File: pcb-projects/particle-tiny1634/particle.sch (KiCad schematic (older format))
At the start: 31 parts, among them CON1 AVR-ISP-6, IC1 ATTINY1634-SU, P1 TXN, P2 RXN, P3 TXS, P4 RXS, P5 TRX-CH, P6 TEST1-3

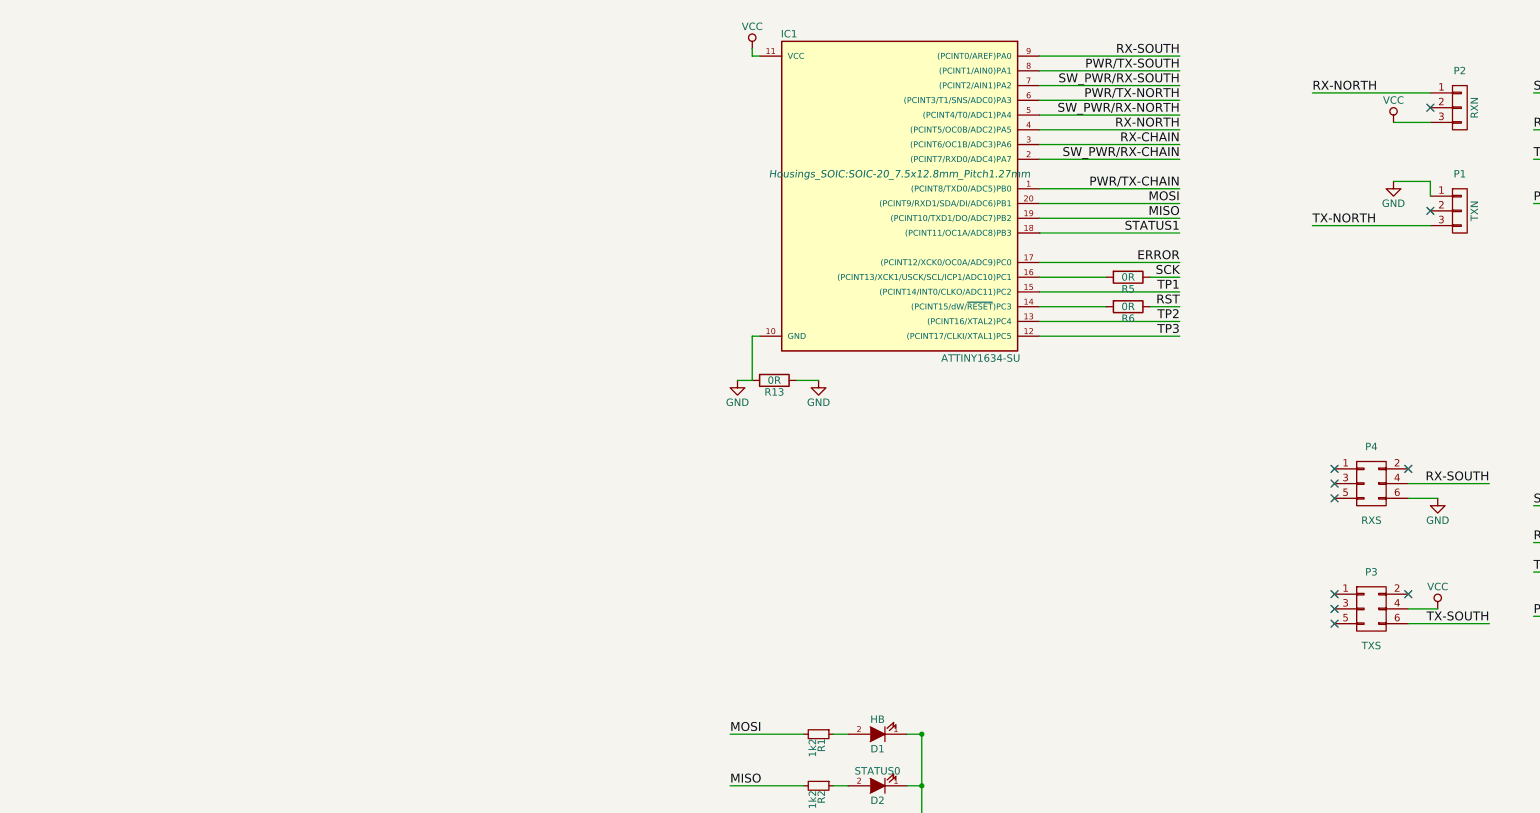
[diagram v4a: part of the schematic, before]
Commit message: minor edge cut alignment, added particle array
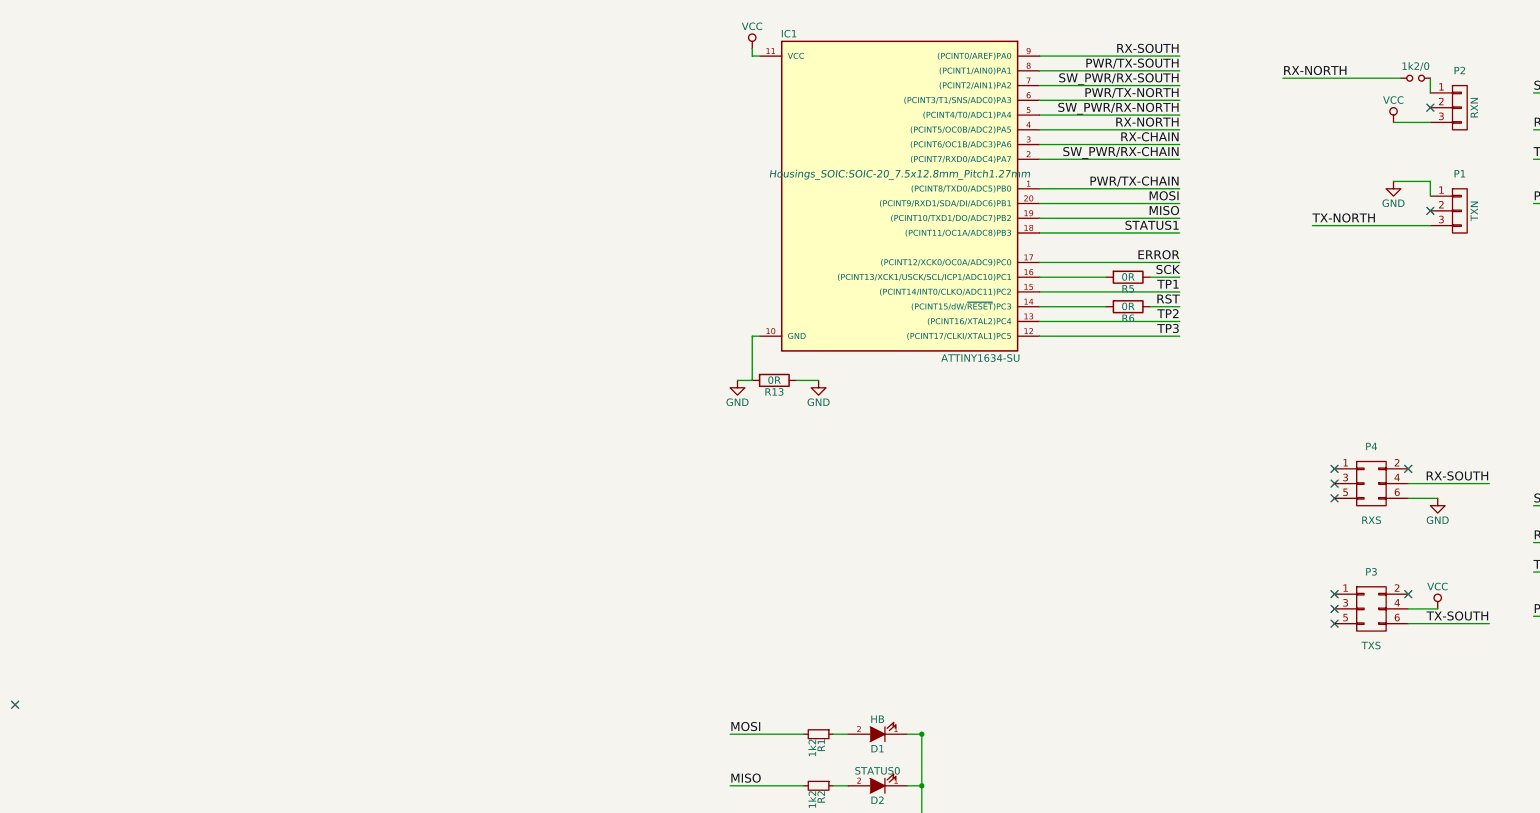
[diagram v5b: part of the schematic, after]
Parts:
- added 1k2/0: 1k2, Resistors_SMD:R_1206, symbol Jumper_NO_Small
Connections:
- net RX-NORTH: now also 1k2/0.1; no longer P2.1 (P1)
- new net: 1k2/0.2, P2.1 (P1)
- no-connect marks 10 -> 11
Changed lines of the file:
@@
 Text Label 4650 2850 0    60   ~ 0
 TX-NORTH
-Text Label 4650 1950 0    60   ~ 0
+Text Label 4450 1850 0    60   ~ 0
 RX-NORTH
 Text Label 8900 3450 0    60   ~ 0
@@
 	5300 5550 5850 5550
 Wire Wire Line
-	4650 1950 5450 1950
+	4450 1850 5250 1850
 Wire Wire Line
 	5200 2150 5450 2150
@@
 NoConn ~ 4800 4700
 NoConn ~ 4800 5450
+$Comp
+L Jumper_NO_Small 1k2/0
+U 1 1 56938DAE
+P 5350 1850
+F 0 "1k2/0" H 5350 1930 50  0000 C CNN
+F 1 "1k2" H 5360 1790 50  0001 C CNN
+F 2 "Resistors_SMD:R_1206" H 5350 1850 50  0001 C CNN
+F 3 "" H 5350 1850 50  0000 C CNN
+	1    5350 1850
+	1    0    0    -1
+$EndComp
+NoConn ~ -4150 6100
+Wire Wire Line
+	5450 1850 5450 1950
 $EndSCHEMATC
